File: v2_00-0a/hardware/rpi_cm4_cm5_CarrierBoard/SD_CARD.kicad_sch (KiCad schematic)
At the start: 17 parts, among them J1 DM3AT-SF-PEJM5, Q4 2N7002, Q5 2N7002, Q6 2N7002, U4 AP22913W6-7

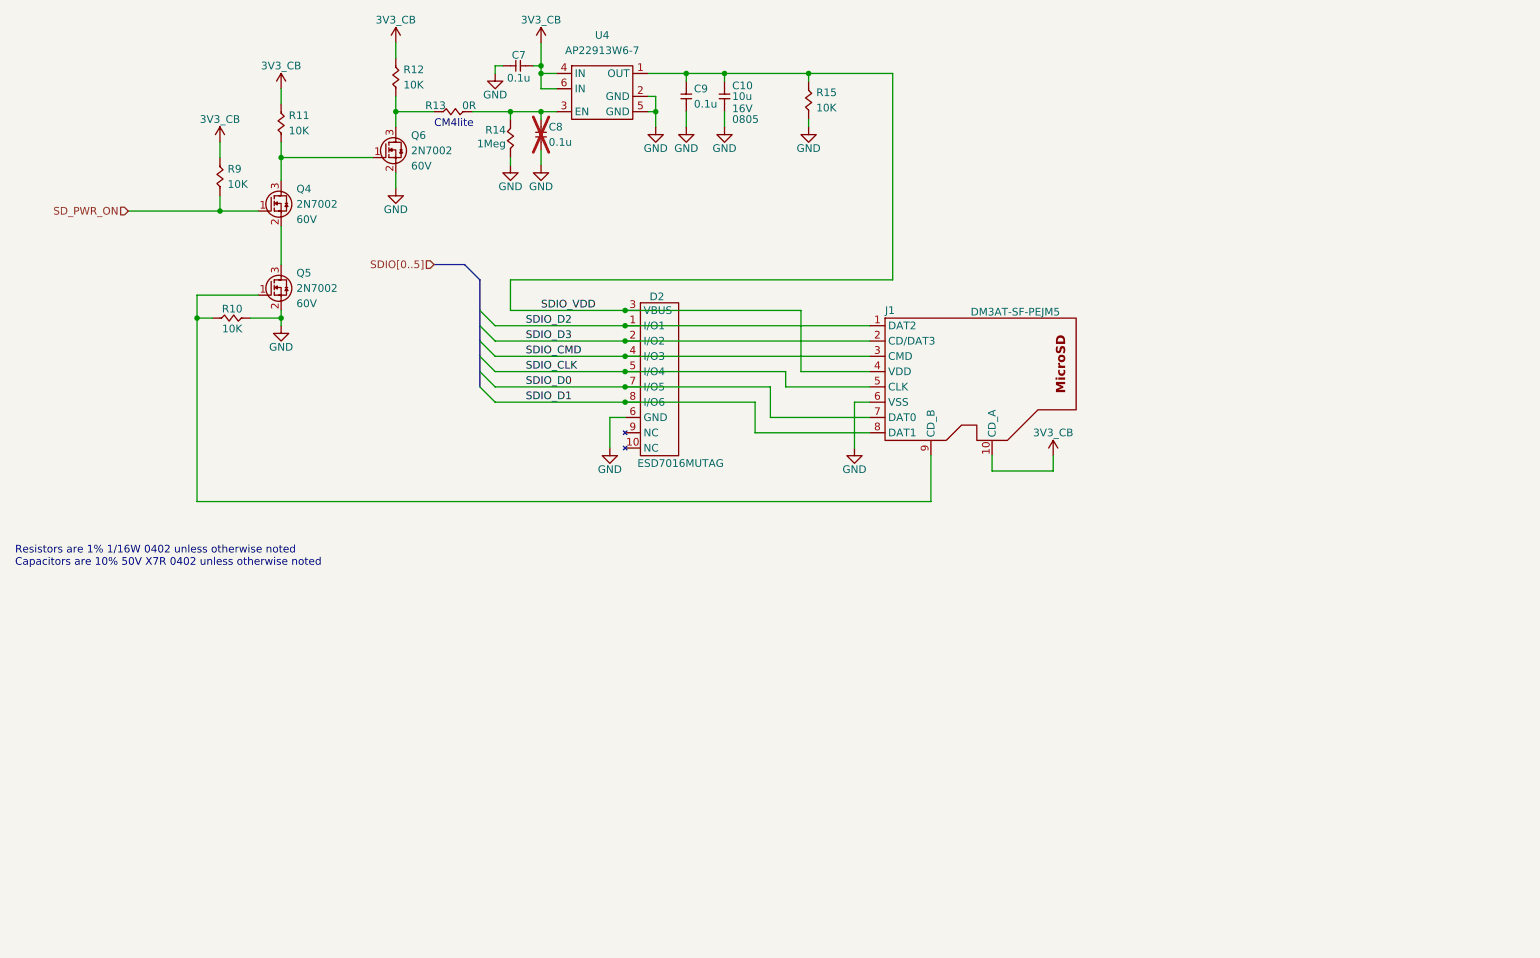
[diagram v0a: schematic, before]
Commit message: Add schematic pages for SOM_CONN_A/B, DSI to LVDS bridge, Ethernet and HDMI
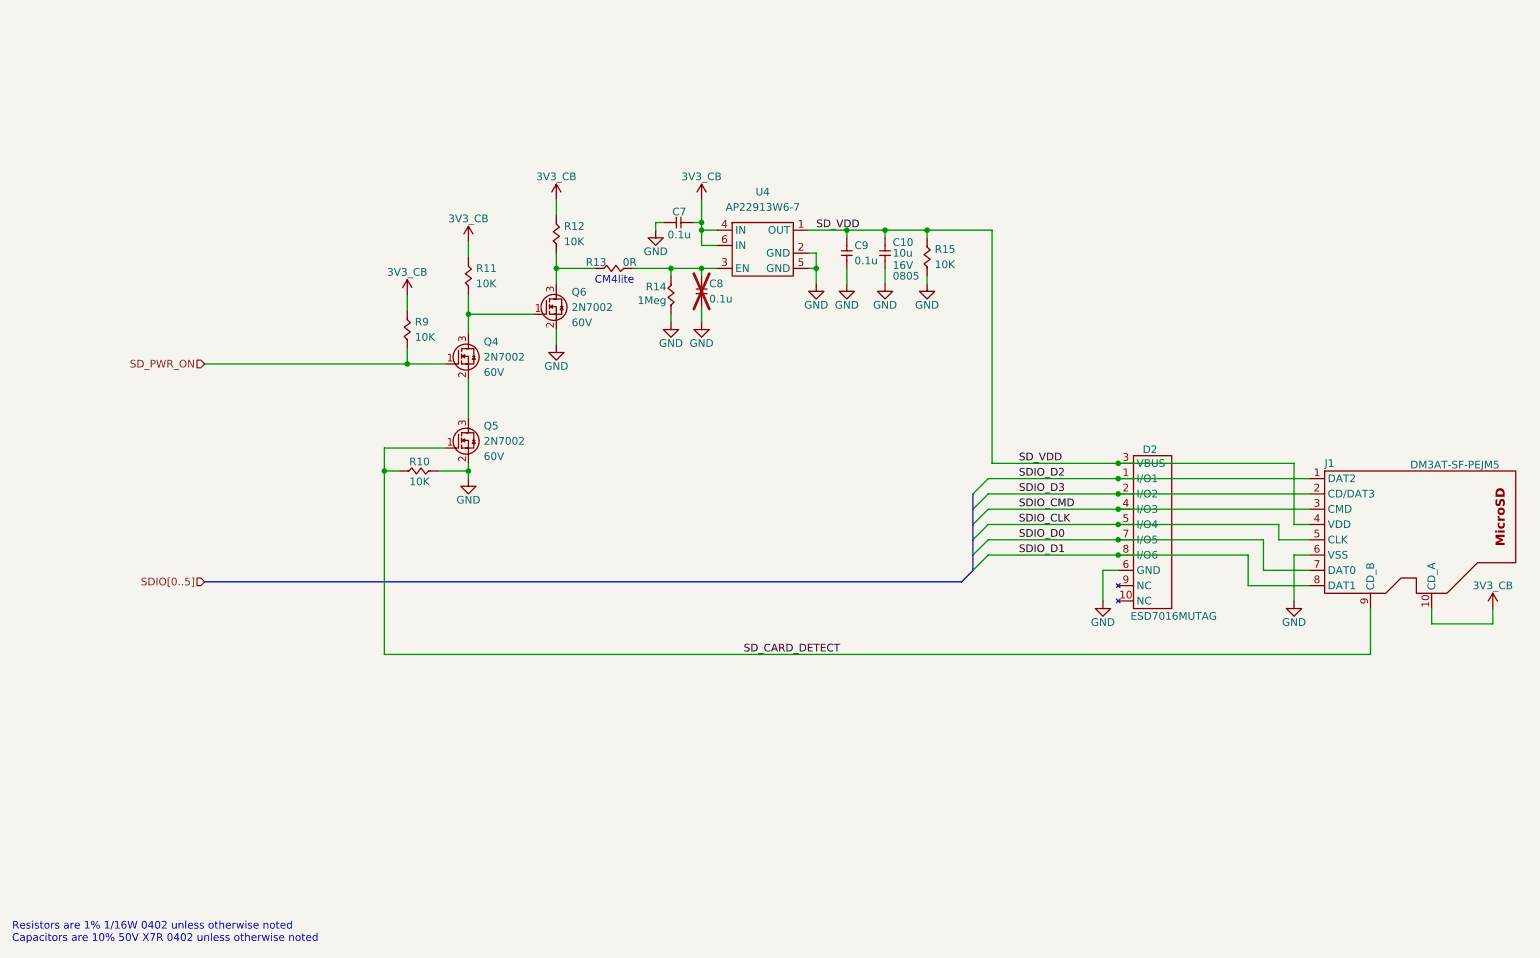
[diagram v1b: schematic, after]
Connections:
- net SD_CARD_DETECT: now reaches J1.9 (CD_B), Q5.1 (G), R10.2
- net SDIO_VDD renamed SD_VDD
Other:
- moved on the sheet: C10, C7, C8, C9, D2, J1, Q4, Q5, Q6, R10, R11, R12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

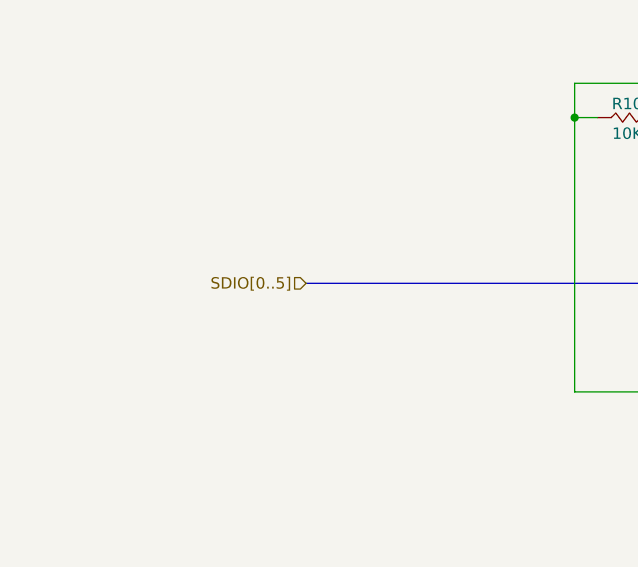
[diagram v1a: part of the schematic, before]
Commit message: Update schematics (several new hierarchical pages, updates bus labels)
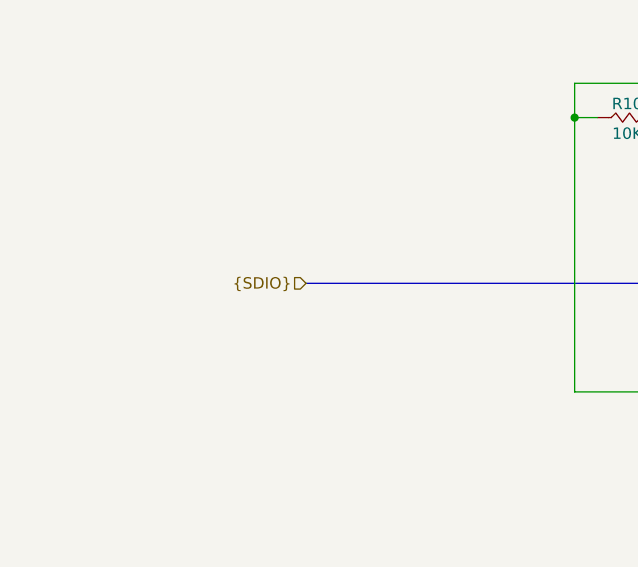
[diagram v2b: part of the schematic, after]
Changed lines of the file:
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@@
 		(comment 8 "WIP")
+	)
+	(bus_alias "SDIO"
+		(members "SDIO_D0" "SDIO_D1" "SDIO_D2" "SDIO_D3" "SDIO_CLK" "SDIO_CMD")
 	)
 	(text "CM4lite"
@@
 		)
 	)
-	(hierarchical_label "SDIO[0..5]"
+	(hierarchical_label "{SDIO}"
 		(shape input)
 		(at 44.45 112.395 180)

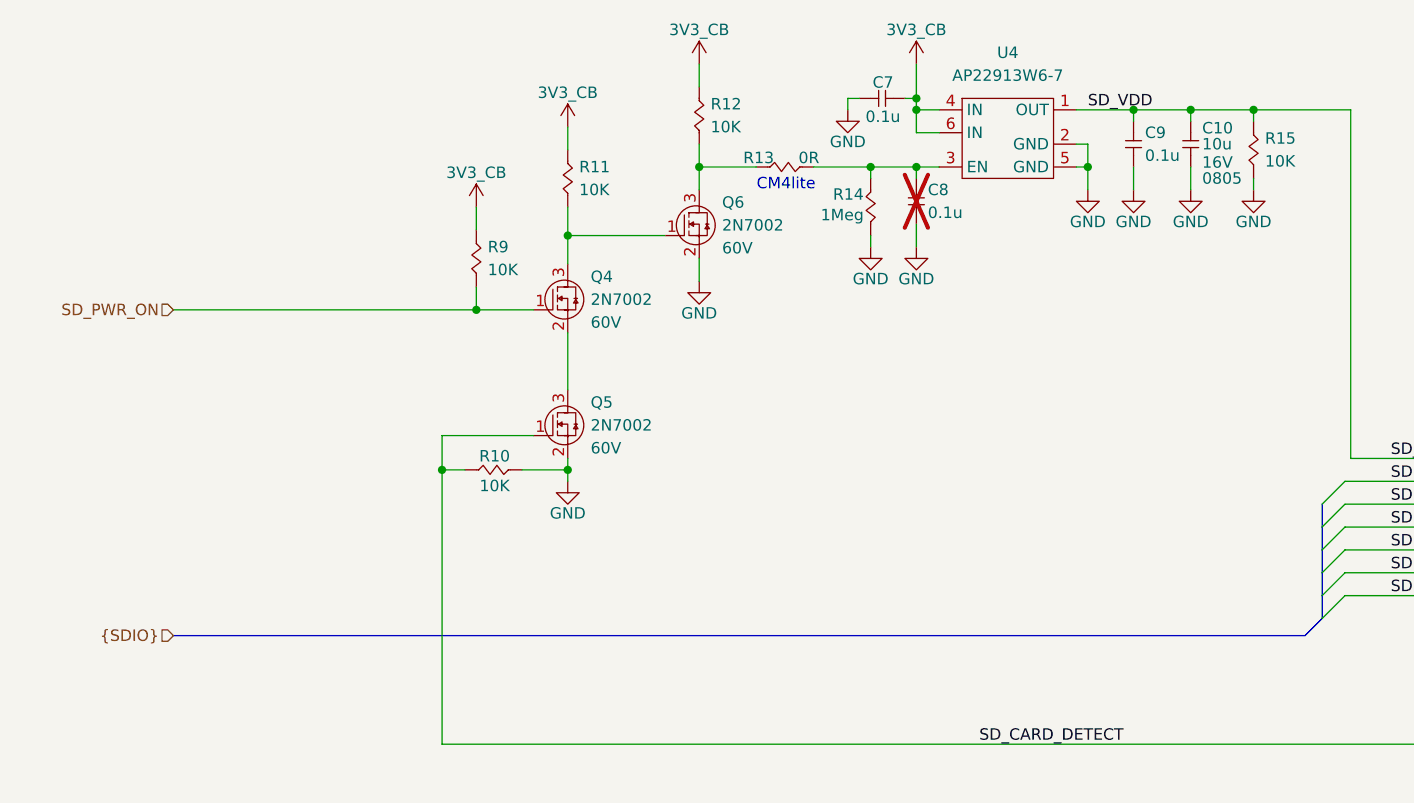
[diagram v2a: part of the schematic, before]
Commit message: Add new page and update schematics
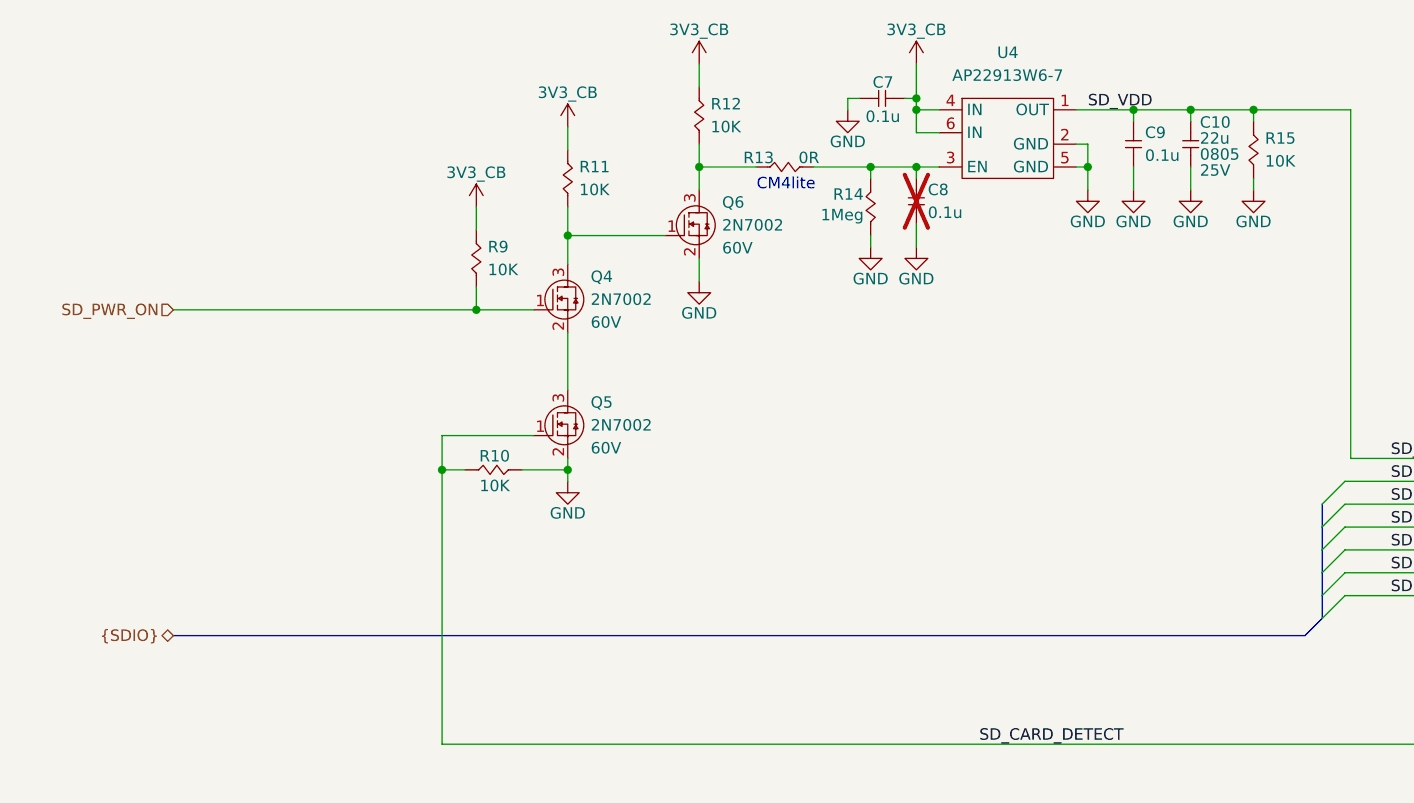
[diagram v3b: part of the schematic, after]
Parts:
- removed C10: 10u, footprint:CAP_NONPOL_0805, symbol KicadCompDb:Capacitors/CAP_CER_SMT_00004
- added C10: 22u, footprint:CAP_NONPOL_0805, symbol KicadCompDb:Capacitors/CAP_CER_SMT_00011
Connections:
- net GND: now also C10.1
- net SD_VDD: now also C10.2
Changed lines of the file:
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@@
 	)
 	(hierarchical_label "{SDIO}"
-		(shape input)
+		(shape bidirectional)
 		(at 44.45 112.395 180)
 		(effects
@@
 				(path "/7dcdf741-90ca-4333-848c-806f4d64158e/adbb075d-f33a-4d25-a8c5-71eb41bbcd81"
 					(reference "#PWR034")
+					(unit 1)
+				)
+			)
+		)
+	)
+	(symbol
+		(lib_id "KicadCompDb:Capacitors/CAP_CER_SMT_00011")
+		(at 157.48 60.325 90)
+		(unit 1)
+		(exclude_from_sim no)
+		(in_bom yes)
+		(on_board yes)
+		(dnp no)
+		(property "Reference" "C10"
+			(at 158.496 55.372 90)
+			(effects
+				(font
+					(size 1.27 1.27)
+				)
+				(justify right)
+			)
+		)
+		(property "Value" "22u"
+			(at 158.496 57.15 90)
+			(effects
+				(font
+					(size 1.27 1.27)
+				)
+				(justify right)
+			)
+		)
+		(property "Footprint" "footprint:CAP_NONPOL_0805"
+			(at 179.578 59.817 0)
+			(effects
+				(font
+					(size 1.27 1.27)
+				)
+				(hide yes)
+			)
+		)
+		(property "Datasheet" "https://mm.digikey.com/Volume0/opasdata/d220001/medias/docus/339/CL21A226MAYNNNE_Spec.pdf"
+			(at 157.48 60.325 0)
+			(effects
+				(font
+					(size 1.27 1.27)
+				)
+				(hide yes)
+			)
+		)
+		(property "Description" "CAP CER 22UF 25V X5R 0805"
+			(at 167.386 58.547 0)
+			(effects
+				(font
+					(size 1.27 1.27)
+				)
+				(hide yes)
+			)
+		)
+		(property "Tolerance" "±20%"
+			(at 177.8 60.071 0)
+			(effects
+				(font
+					(size 1.27 1.27)
+				)
+				(hide yes)
+			)
+		)
+		(property "Dielectric" "X5R"
+			(at 171.704 60.071 0)
+			(effects
+				(font
+					(size 1.27 1.27)
+				)
+				(hide yes)
+			)
+		)
+		(property "Package" "0805"
+			(at 158.496 58.928 90)
+			(effects
+				(font
+					(size 1.27 1.27)
+				)
+				(justify right)
+			)
+		)
+		(property "Operating Temperature" "-55°C ~ 85°C"
+			(at 181.864 59.563 0)
+			(effects
+				(font
+					(size 1.27 1.27)
+				)
+				(hide yes)
+			)
+		)
+		(property "Voltage Rating" "25V"
+			(at 158.496 60.706 90)
+			(effects
+				(font
+					(size 1.27 1.27)
+				)
+				(justify right)
+			)
+		)
+		(property "Manufacturer" "Samsung Electro-Mechanics"
+			(at 175.768 60.071 0)
+			(effects
+				(font
+					(size 1.27 1.27)
+				)
+				(hide yes)
+			)
+		)
+		(property "Manufacturer Part Number" "CL21A226MAYNNNE"
+			(at 165.354 60.071 0)
+			(effects
+				(font
+					(size 1.27 1.27)
+				)
+				(hide yes)
+			)
+		)
+		(property "Distributor" "DigiKey"
+			(at 163.322 60.325 0)
+			(effects
+				(font
+					(size 1.27 1.27)
+				)
+				(hide yes)
+			)
+		)
+		(property "Distributor Part Number" "1276-CL21A226MAYNNNECT-ND"
+			(at 169.672 59.563 0)
+			(effects
+				(font
+					(size 1.27 1.27)
+				)
+				(hide yes)
+			)
+		)
+		(property "Type" "CER SMT"
+			(at 157.48 60.325 0)
+			(show_name yes)
+			(effects
+				(font
+					(size 1.27 1.27)
+				)
+				(hide yes)
+			)
+		)
+		(property "Dimensions" "2.00mm x 1.25mm"
+			(at 157.48 60.325 0)
+			(show_name yes)
+			(effects
+				(font
+					(size 1.27 1.27)
+				)
+				(hide yes)
+			)
+		)
+		(pin "1"
+		)
+		(pin "2"
+		)
+		(instances
+			(project "rpi_cm4_cm5_CarrierBoard"
+				(path "/7dcdf741-90ca-4333-848c-806f4d64158e/adbb075d-f33a-4d25-a8c5-71eb41bbcd81"
+					(reference "C10")
 					(unit 1)
 				)
@@
 					(unit 1)
 				)
-			)
-		)
-	)
-	(symbol
-		(lib_id "KicadCompDb:Capacitors/CAP_CER_SMT_00004")
-		(at 157.48 60.325 90)
-		(unit 1)
-		(exclude_from_sim no)
-		(in_bom yes)
-		(on_board yes)
-		(dnp no)
-		(property "Reference" "C10"
-			(at 158.75 56.007 90)
-			(effects
-				(font
-					(size 1.27 1.27)
-				)
-				(justify right)
-			)
-		)
-		(property "Value" "10u"
-			(at 158.75 57.785 90)
-			(effects
-				(font
-					(size 1.27 1.27)
-				)
-				(justify right)
-			)
-		)
-		(property "Footprint" "footprint:CAP_NONPOL_0805"
-			(at 179.578 59.817 0)
-			(effects
-				(font
-					(size 1.27 1.27)
-				)
-				(hide yes)
-			)
-		)
-		(property "Datasheet" "https://mm.digikey.com/Volume0/opasdata/d220001/medias/docus/609/CL21A106KOQNNNE_Spec.pdf"
-			(at 157.48 60.325 0)
-			(effects
-				(font
-					(size 1.27 1.27)
-				)
-				(hide yes)
-			)
-		)
-		(property "Description" "CAP CER 10UF 16V X5R 0805"
-			(at 167.386 58.547 0)
-			(effects
-				(font
-					(size 1.27 1.27)
-				)
-				(hide yes)
-			)
-		)
-		(property "Tolerance" "±10%"
-			(at 177.8 60.071 0)
-			(effects
-				(font
-					(size 1.27 1.27)
-				)
-				(hide yes)
-			)
-		)
-		(property "Dielectric" "X5R"
-			(at 171.704 60.071 0)
-			(effects
-				(font
-					(size 1.27 1.27)
-				)
-				(hide yes)
-			)
-		)
-		(property "Package" "0805"
-			(at 158.75 61.595 90)
-			(effects
-				(font
-					(size 1.27 1.27)
-				)
-				(justify right)
-			)
-		)
-		(property "Operating Temperature" "-55°C ~ 85°C"
-			(at 181.864 59.563 0)
-			(effects
-				(font
-					(size 1.27 1.27)
-				)
-				(hide yes)
-			)
-		)
-		(property "Voltage Rating" "16V"
-			(at 158.75 59.817 90)
-			(effects
-				(font
-					(size 1.27 1.27)
-				)
-				(justify right)
-			)
-		)
-		(property "Manufacturer" "Samsung Electro-Mechanics"
-			(at 175.768 60.071 0)
-			(effects
-				(font
-					(size 1.27 1.27)
-				)
-				(hide yes)
-			)
-		)
-		(property "Manufacturer Part Number" "CL21A106KOQNNNE"
-			(at 165.354 60.071 0)
-			(effects
-				(font
-					(size 1.27 1.27)
-				)
-				(hide yes)
-			)
-		)
-		(property "Distributor" "DigiKey"
-			(at 163.322 60.325 0)
-			(effects
-				(font
-					(size 1.27 1.27)
-				)
-				(hide yes)
-			)
-		)
-		(property "Distributor Part Number" "1276-1096-1-ND"
-			(at 169.672 59.563 0)
-			(effects
-				(font
-					(size 1.27 1.27)
-				)
-				(hide yes)
-			)
-		)
-		(property "Type" "CER SMT"
-			(at 157.48 60.325 0)
-			(show_name yes)
-			(effects
-				(font
-					(size 1.27 1.27)
-				)
-				(hide yes)
-			)
-		)
-		(property "Dimensions" "2.00mm x 1.25mm"
-			(at 157.48 60.325 0)
-			(show_name yes)
-			(effects
-				(font
-					(size 1.27 1.27)
-				)
-				(hide yes)
-			)
-		)
-		(pin "2"
-		)
-		(pin "1"
-		)
-		(instances
-			(project ""
-				(path "/7dcdf741-90ca-4333-848c-806f4d64158e/adbb075d-f33a-4d25-a8c5-71eb41bbcd81"
-					(reference "C10")
-					(unit 1)
-				)
